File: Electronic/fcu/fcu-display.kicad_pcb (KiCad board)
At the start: 2 copper layers, 34 parts, among them U101 Connector-FPC-50pins

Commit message: Update fcu schemas and libraries
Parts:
- removed ALT201, ALT202, ALT203, ALT204, ALT205, HDG301, HDG302, HDG303, SPEED201, SPEED202, SPEED203, VS301, VS302, VS303, VS304, VS305: HDSP-7403, Display_7Segment:HDSP-7401
- added ALT1: HDSP-7401, Display_7Segment:HDSP-7401, F.Cu at (171.4, 63.5)
- added ALT2: HDSP-7401, Display_7Segment:HDSP-7401, F.Cu at (179.7, 63.5)
- added ALT3: HDSP-7401, Display_7Segment:HDSP-7401, F.Cu at (188.0, 63.5)
- added ALT4: HDSP-7401, Display_7Segment:HDSP-7401, F.Cu at (196.2, 63.5)
- added ALT5: HDSP-7401, Display_7Segment:HDSP-7401, F.Cu at (204.5, 63.5)
- added HDG1: HDSP-7401, Display_7Segment:HDSP-7401, F.Cu at (98.4, 63.5)
- added HDG2: HDSP-7401, Display_7Segment:HDSP-7401, F.Cu at (106.7, 63.5)
- added HDG3: HDSP-7401, Display_7Segment:HDSP-7401, F.Cu at (114.9, 63.5)
- added SPEED1: HDSP-7401, Display_7Segment:HDSP-7401, F.Cu at (61.0, 63.5)
- added SPEED2: HDSP-7401, Display_7Segment:HDSP-7401, F.Cu at (69.2, 63.5)
- added SPEED3: HDSP-7401, Display_7Segment:HDSP-7401, F.Cu at (77.5, 63.5)
- added VS1: HDSP-7401, Display_7Segment:HDSP-7401, F.Cu at (216.5, 63.5)
- added VS2: HDSP-7401, Display_7Segment:HDSP-7401, F.Cu at (224.8, 63.5)
- added VS3: HDSP-7401, Display_7Segment:HDSP-7401, F.Cu at (233.0, 63.5)
- added VS4: HDSP-7401, Display_7Segment:HDSP-7401, F.Cu at (241.3, 63.5)
- added VS5: HDSP-7401, Display_7Segment:HDSP-7401, F.Cu at (249.6, 63.5)
- moved DAltManaged401 0.64 mm to (212.7, 69.8)
- renumbered PadALT401 to PadALT1, PaveFPA401 to PadFPA1, PaveFPA402 to PadFPA2, PaveHDG401 to PadHDG1, PaveHDG402 to PadHDG2, PadLVLCH401 to PadLVLCH1, PadLine401 to PadLine1, PadLine402 to PadLine2, PaveMach401 to PadMach1, PaveSpeed401 to PadSpeed1, PaveTRK401 to PadTRK1, PaveTRK402 to PadTRK2, PaveVS401 to PadVS1, PaveVS402 to PadVS2
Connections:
- PadSpeed1 pad 3: Dr3SegA -> Net-(PadSpeed1-Pad3)
- PadSpeed1 pad 6: Dr3SegA -> Net-(PadSpeed1-Pad3)
- U101 pad 1: hdgVsDig3 -> Net-(U101-Pad1)
- U101 pad 10: Dr3Dig5 -> Dr3Dig0
- U101 pad 11: Dr3Dig6 -> Dr3SegDP
- U101 pad 12: Dr3Dig7 -> Dr3SegG
- U101 pad 13: speedAltDig3 -> Dr3SegF
- U101 pad 14: speedAltDig4 -> Dr3SegE
- U101 pad 15: speedAltDig5 -> Dr3SegD
- U101 pad 16: speedAltDig6 -> Dr3SegC
- U101 pad 17: speedAltDig7 -> Dr3SegB
- U101 pad 18: hdgVsB -> Dr3SegA
- U101 pad 19: hdgVsC -> speedAltE
- U101 pad 2: hdgVsDig4 -> Net-(U101-Pad2)
- U101 pad 20: hdgVsD -> speedAltD
- U101 pad 21: hdgVsE -> speedAltC
- U101 pad 22: hdgVsF -> speedAltB
- U101 pad 23: hdgVsG -> speedAltA
- U101 pad 24: hdgVsDP -> hdgVsDig2
- U101 pad 25: hdgVsDig0 -> hdgVsDig1
- U101 pad 26: hdgVsDig1 -> hdgVsDig0
- U101 pad 27: hdgVsDig2 -> hdgVsDP
- U101 pad 28: speedAltA -> hdgVsG
- U101 pad 29: speedAltB -> hdgVsF
- U101 pad 3: hdgVsDig5 -> speedAltDig2
- U101 pad 30: speedAltC -> hdgVsE
- U101 pad 31: speedAltD -> hdgVsD
- U101 pad 32: speedAltE -> hdgVsC
- U101 pad 33: Dr3SegA -> hdgVsB
- U101 pad 34: Dr3SegB -> speedAltDig7
- U101 pad 35: Dr3SegC -> speedAltDig6
- U101 pad 36: Dr3SegD -> speedAltDig5
- U101 pad 37: Dr3SegE -> speedAltDig4
- U101 pad 38: Dr3SegF -> speedAltDig3
- U101 pad 39: Dr3SegG -> Dr3Dig7
- U101 pad 4: hdgVsDig6 -> speedAltDig1
- U101 pad 40: Dr3SegDP -> Dr3Dig6
- U101 pad 41: Dr3Dig0 -> Dr3Dig5
- U101 pad 42: Dr3Dig1 -> speedAltDP
- U101 pad 43: Dr3Dig2 -> speedAltG
- U101 pad 44: Dr3Dig3 -> speedAltF
- U101 pad 45: Dr3Dig4 -> hdgVsA
- U101 pad 46: speedAltDig0 -> hdgVsDig7
- U101 pad 47: speedAltDig1 -> hdgVsDig6
- U101 pad 48: speedAltDig2 -> hdgVsDig5
- U101 pad 49: Net-(U101-Pad49) -> hdgVsDig4
- U101 pad 5: hdgVsDig7 -> speedAltDig0
- U101 pad 50: Net-(U101-Pad50) -> hdgVsDig3
- U101 pad 6: hdgVsA -> Dr3Dig4
- U101 pad 7: speedAltF -> Dr3Dig3
- U101 pad 8: speedAltG -> Dr3Dig2
- U101 pad 9: speedAltDP -> Dr3Dig1
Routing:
- net Dr3Dig0: track 369.3 -> 0.00 mm
- net speedAltF: track 218.3 -> 0.00 mm, vias 1 -> 0
- net hdgVsA: track 214.8 -> 0.00 mm, vias 1 -> 0
- net Dr3Dig1: track 214.1 -> 0.00 mm, vias 1 -> 0
- net hdgVsD: track 205.8 -> 0.00 mm, vias 2 -> 0
- net hdgVsF: track 204.3 -> 0.00 mm, vias 2 -> 0
- net Dr3SegF: track 198.4 -> 0.00 mm, vias 1 -> 0
- net hdgVsC: track 198.4 -> 0.00 mm
- net hdgVsG: track 197.0 -> 0.00 mm, vias 2 -> 0
- net hdgVsDP: track 194.1 -> 0.00 mm, vias 2 -> 0
- net hdgVsE: track 192.3 -> 0.00 mm, vias 2 -> 0
- net hdgVsB: track 191.7 -> 0.00 mm
- net speedAltG: track 184.0 -> 0.00 mm, vias 1 -> 0
- net speedAltD: track 176.2 -> 0.00 mm, vias 1 -> 0
- net speedAltC: track 175.0 -> 0.00 mm, vias 1 -> 0
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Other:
- board outline added: 205 x 30 mm
- board text added: "HomeCockpit A320 - VirtualGit FCU Display - V1.0 - 17/02/2021"

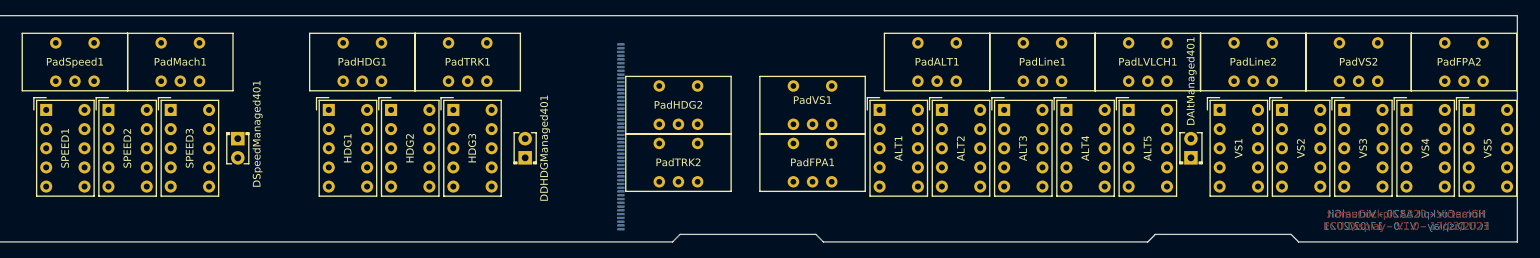
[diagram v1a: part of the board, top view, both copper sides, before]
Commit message: Update FCU display board with routing
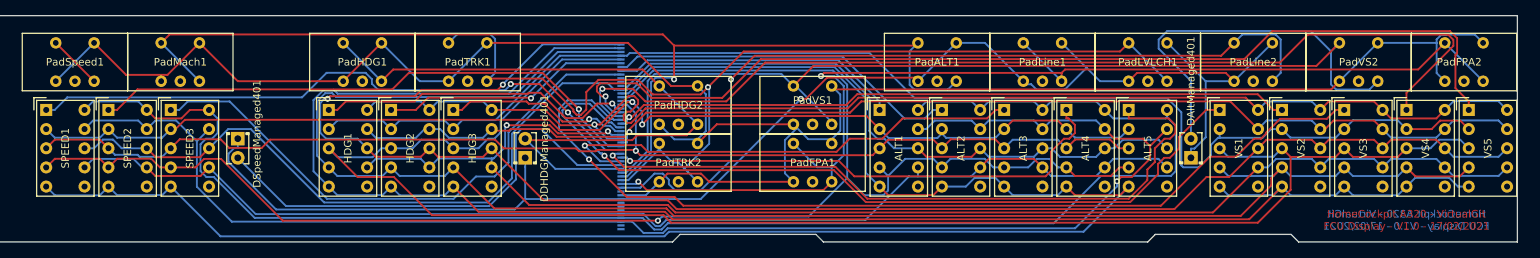
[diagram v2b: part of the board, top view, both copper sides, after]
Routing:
- net Dr3Dig0: track 0.00 -> 273.5 mm
- net speedAltDig4: track 0.00 -> 235.9 mm
- net hdgVsDig4: track 0.00 -> 225.0 mm
- net hdgVsDig5: track 0.00 -> 223.8 mm
- net hdgVsDig7: track 0.00 -> 221.0 mm
- net hdgVsDig3: track 0.00 -> 217.6 mm, vias 0 -> 2
- net speedAltDig1: track 0.00 -> 209.0 mm
- net speedAltDig5: track 0.00 -> 205.4 mm, vias 0 -> 1
- net speedAltDig2: track 0.00 -> 198.5 mm, vias 0 -> 1
- net Dr3Dig1: track 0.00 -> 194.3 mm, vias 0 -> 1
- net hdgVsDig0: track 0.00 -> 183.7 mm, vias 0 -> 2
- net hdgVsDig6: track 0.00 -> 174.5 mm
- net speedAltDig3: track 0.00 -> 173.5 mm
- net hdgVsDig1: track 0.00 -> 171.6 mm, vias 0 -> 1
- net Dr3SegC: track 0.00 -> 168.8 mm
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
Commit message: Adust fcu display pcb layout Add Vcc to rotary encoder and update pcb with jst +1 pin
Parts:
- moved PadMach1 8.98 mm to (69.8, 58.4)
- moved PadSpeed1 8.98 mm to (55.9, 58.4)
- moved PadFPA2 8.28 mm to (257.2, 57.8)
- moved PadLine2 8.28 mm to (229.2, 57.8)
- moved PadVS2 8.28 mm to (243.2, 57.8)
- moved PadALT1 8.28 mm to (187.3, 57.8)
- moved PadLVLCH1 8.28 mm to (215.3, 57.8)
- moved PadLine1 8.28 mm to (201.3, 57.8)
- moved SPEED2 7.62 mm to (61.6, 63.5)
- moved SPEED3 7.62 mm to (69.8, 63.5)
- moved SPEED1 7.62 mm to (53.3, 63.5)
- moved DSpeedManaged401 6.98 mm to (79.4, 67.3)
- moved VS3 6.35 mm to (239.4, 63.5)
- moved VS1 6.35 mm to (222.9, 63.5)
- moved VS2 6.35 mm to (231.1, 63.5)
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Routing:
- net Dr3Dig0: track 273.5 -> 0.00 mm
- net speedAltDig4: track 235.9 -> 0.00 mm
- net hdgVsDig4: track 225.0 -> 0.00 mm
- net hdgVsDig5: track 223.8 -> 0.00 mm
- net hdgVsDig7: track 221.0 -> 0.00 mm
- net hdgVsDig3: track 217.6 -> 0.00 mm, vias 2 -> 0
- net speedAltDig1: track 209.0 -> 0.00 mm
- net speedAltDig5: track 205.4 -> 0.00 mm, vias 1 -> 0
- net speedAltDig2: track 198.5 -> 0.00 mm, vias 1 -> 0
- net Dr3Dig1: track 194.3 -> 0.00 mm, vias 1 -> 0
- net hdgVsDig0: track 183.7 -> 0.00 mm, vias 2 -> 0
- net hdgVsDig6: track 174.5 -> 0.00 mm
- net speedAltDig3: track 173.5 -> 0.00 mm
- net hdgVsDig1: track 171.6 -> 0.00 mm, vias 1 -> 0
- net Dr3SegC: track 168.8 -> 0.00 mm
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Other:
- board size 205 x 30 mm -> 238 x 28 mm
- board text added: "HomeCockpit A320 - VirtualGit - FCU Display - V1.0 - 17/02/2021"
- board text removed: "HomeCockpit A320 - VirtualGit FCU Display - V1.0 - 17/02/2021"

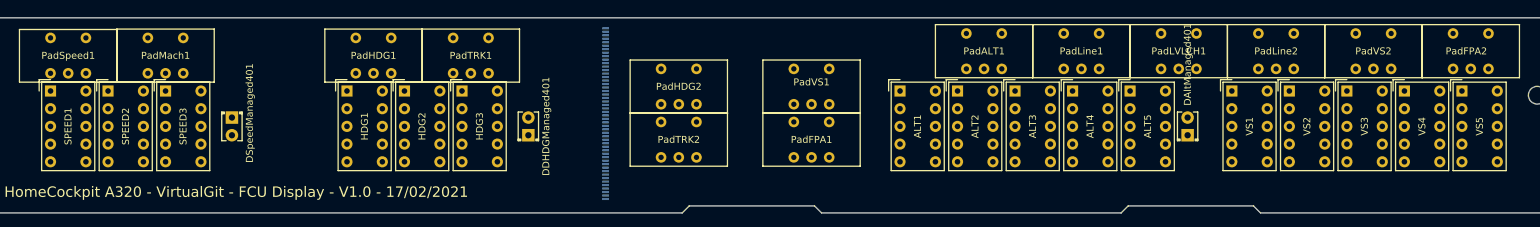
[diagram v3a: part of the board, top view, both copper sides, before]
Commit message: Update FCU PCB net routing
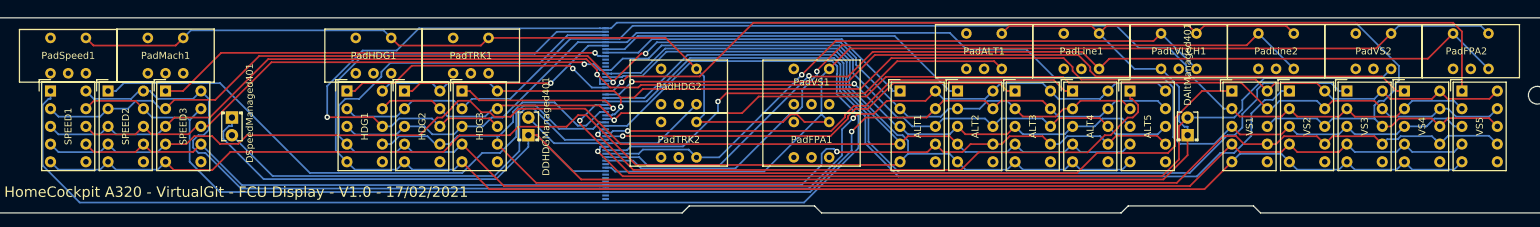
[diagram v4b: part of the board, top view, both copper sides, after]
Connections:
- PadALT1 pad 3: Dr3SegD -> Net-(PadALT1-Pad3)
- PadALT1 pad 4: Dr3Dig1 -> Net-(PadALT1-Pad4)
- PadFPA1 pad 3: Dr3SegF -> Net-(PadFPA1-Pad3)
- PadFPA1 pad 4: Dr3Dig0 -> Net-(PadFPA1-Pad4)
- PadFPA1 pad 6: Dr3SegF -> Net-(PadFPA1-Pad6)
- PadFPA2 pad 4: Dr3Dig0 -> Net-(PadFPA2-Pad4)
- PadHDG1 pad 3: Dr3SegB -> Net-(PadHDG1-Pad3)
- PadHDG1 pad 4: Dr3Dig0 -> Net-(PadHDG1-Pad4)
- PadHDG1 pad 6: Dr3SegB -> Net-(PadHDG1-Pad6)
- PadHDG2 pad 3: Dr3SegB -> Net-(PadHDG2-Pad3)
- PadHDG2 pad 4: Dr3Dig0 -> Net-(PadHDG2-Pad4)
- PadLine1 pad 3: Dr3SegF -> Net-(PadLine1-Pad3)
- PadLine1 pad 4: Dr3Dig1 -> Net-(PadLine1-Pad4)
- PadLine2 pad 4: Dr3Dig1 -> Net-(PadLine2-Pad4)
- PadMach1 pad 3: Dr3SegD -> Net-(PadMach1-Pad3)
- PadMach1 pad 4: Dr3Dig0 -> Net-(PadMach1-Pad4)
- PadMach1 pad 6: Dr3SegD -> Net-(PadMach1-Pad6)
- PadSpeed1 pad 4: Dr3Dig0 -> Net-(PadSpeed1-Pad4)
- PadSpeed1 pad 6: Net-(PadSpeed1-Pad3) -> Net-(PadSpeed1-Pad6)
- PadTRK1 pad 3: Dr3SegE -> Net-(PadTRK1-Pad3)
- PadTRK1 pad 4: Dr3Dig0 -> Net-(PadTRK1-Pad4)
- PadTRK1 pad 6: Dr3SegE -> Net-(PadTRK1-Pad6)
- PadTRK2 pad 3: Dr3SegE -> Net-(PadTRK2-Pad3)
- PadTRK2 pad 4: Dr3Dig0 -> Net-(PadTRK2-Pad4)
- PadVS1 pad 3: Dr3SegC -> Net-(PadVS1-Pad3)
- PadVS1 pad 4: Dr3Dig0 -> Net-(PadVS1-Pad4)
- PadVS1 pad 6: Dr3SegC -> Net-(PadVS1-Pad6)
- PadVS2 pad 3: Dr3SegC -> Net-(PadVS2-Pad3)
- PadVS2 pad 4: Dr3Dig0 -> Net-(PadVS2-Pad4)
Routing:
- net Dr3Dig0: track 0.00 -> 261.4 mm
- net hdgVsDig3: track 0.00 -> 237.7 mm, vias 0 -> 1
- net Dr3Dig1: track 0.00 -> 235.3 mm
- net hdgVsDig4: track 0.00 -> 222.7 mm
- net speedAltDig4: track 0.00 -> 222.1 mm
- net hdgVsDig5: track 0.00 -> 219.5 mm
- net speedAltDig5: track 0.00 -> 219.5 mm
- net hdgVsDig0: track 0.00 -> 192.5 mm
- net speedAltB: track 0.00 -> 184.3 mm
- net hdgVsDig7: track 0.00 -> 183.0 mm
- net speedAltDig1: track 0.00 -> 182.0 mm, vias 0 -> 1
- net speedAltDig2: track 0.00 -> 176.9 mm, vias 0 -> 1
- net hdgVsDig6: track 0.00 -> 176.3 mm
- net hdgVsDig1: track 0.00 -> 174.8 mm, vias 0 -> 1
- net speedAltDig6: track 0.00 -> 173.4 mm, vias 0 -> 2
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
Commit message: Finalise first FCU PCB version
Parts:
- moved PadHDG1 0.64 mm to (99.7, 57.8)
- moved PadMach1 0.64 mm to (69.8, 57.8)
- moved PadSpeed1 0.64 mm to (55.9, 57.8)
- moved PadTRK1 0.64 mm to (113.7, 57.8)
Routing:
- net hdgVsDig7: track 183.0 -> 292.7 mm
- net speedAltB: track 184.3 -> 102.4 mm, vias 0 -> 1
- net hdgVsDig6: track 176.3 -> 231.1 mm, vias 0 -> 1
- net Dr3SegF: track 139.2 -> 187.6 mm
- net hdgVsDig3: track 237.7 -> 275.8 mm, vias 1 -> 0
- net Dr3Dig1: track 235.3 -> 211.6 mm, vias 0 -> 1
- net hdgVsDig2: track 172.5 -> 192.5 mm, vias 1 -> 0
- net Dr3Dig0: track 261.4 -> 276.2 mm
- net hdgVsDig5: track 219.5 -> 205.7 mm, vias 0 -> 1
- net speedAltDig3: track 172.3 -> 186.0 mm
- net hdgVsDig0: track 192.5 -> 179.7 mm, vias 0 -> 2
- net Dr3SegB: track 28.0 -> 37.5 mm
- net speedAltA: track 84.9 -> 94.5 mm
- net speedAltC: track 88.5 -> 80.3 mm
- net Dr3SegG: track 111.2 -> 117.9 mm
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- added copper zone on B.Cu, net (none)
- added copper zone on F.Cu, net (none)

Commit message: Update electornic schema of FCU MotherBoard and Display. Replace MAX7219 for leds to dedicated TLC5917.
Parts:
- removed U101: Connector-FPC-50pins, home-cockpit-footprints:Connector-FPC-50pins-0.5mm
- added DisplayConnector1: Connector-FPC-50pins, home-cockpit-footprints:Connector-FPC-50pins-0.5mm, B.Cu at (136.5, 66.7)
- added PadLAT1: LedPad, home-cockpit-footprints:PadLed-KingBright-DE-2YD, F.Cu at (123.2, 57.8)
- PadALT1, PadFPA1, PadFPA2, PadHDG1, PadHDG2, PadLVLCH1, PadLine1, PadLine2, PadMach1, PadSpeed1, PadTRK1, PadTRK2, PadVS1, PadVS2: value LedPave-home-cockpit-library -> LedPad
- moved PadTRK1 4.45 mm to (109.2, 57.8)
- moved PadHDG1 4.44 mm to (95.2, 57.8)
- moved DSpeedManaged401 1.91 mm to (79.4, 69.2), turned to 90 degrees
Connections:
- DAltManaged401 pad 1: Dr3Dig1 -> LedManagedALT
- DAltManaged401 pad 2: Dr3SegC -> Vcc12V
- DDHDGManaged401 pad 1: Dr3Dig1 -> LedManagedHDG
- DDHDGManaged401 pad 2: Dr3SegB -> Vcc12V
- DSpeedManaged401 pad 1: Dr3Dig1 -> LedManagedSpeed
- DSpeedManaged401 pad 2: Dr3SegA -> Vcc12V
- PadALT1 pad 1: Dr3Dig1 -> Net-(PadALT1-Pad1)
- PadALT1 pad 3: Net-(PadALT1-Pad3) -> Vcc12V
- PadALT1 pad 6: Dr3SegD -> Net-(PadALT1-Pad4)
- PadFPA1 pad 1: Dr3Dig0 -> Net-(PadFPA1-Pad1)
- PadFPA1 pad 3: Net-(PadFPA1-Pad3) -> Vcc12V
- PadFPA1 pad 6: Net-(PadFPA1-Pad6) -> Net-(PadFPA1-Pad4)
- PadFPA2 pad 1: Dr3Dig0 -> LedPadFPA
- PadFPA2 pad 3: Dr3SegF -> Net-(PadFPA1-Pad1)
- PadFPA2 pad 6: Dr3SegF -> Net-(PadFPA2-Pad4)
- PadHDG1 pad 1: Dr3Dig0 -> Net-(PadHDG1-Pad1)
- PadHDG1 pad 3: Net-(PadHDG1-Pad3) -> Vcc12V
- PadHDG1 pad 6: Net-(PadHDG1-Pad6) -> Net-(PadHDG1-Pad4)
- PadHDG2 pad 1: Dr3Dig0 -> LedPadHDG
- PadHDG2 pad 3: Net-(PadHDG2-Pad3) -> Net-(PadHDG1-Pad1)
- PadHDG2 pad 6: Dr3SegB -> Net-(PadHDG2-Pad4)
- PadLVLCH1 pad 1: Dr3Dig1 -> LedPadStaticALT
- PadLVLCH1 pad 3: Dr3SegE -> Net-(PadALT1-Pad1)
- PadLVLCH1 pad 4: Dr3Dig1 -> Net-(PadLVLCH1-Pad4)
- PadLVLCH1 pad 6: Dr3SegE -> Net-(PadLVLCH1-Pad4)
- PadLine1 pad 1: Dr3Dig1 -> Net-(PadLine1-Pad1)
- PadLine1 pad 3: Net-(PadLine1-Pad3) -> Vcc12V
- PadLine1 pad 6: Dr3SegF -> Net-(PadLine1-Pad4)
- PadLine2 pad 1: Dr3Dig1 -> LedPadStaticLines
- PadLine2 pad 3: Dr3SegG -> Net-(PadLine1-Pad1)
- PadLine2 pad 6: Dr3SegG -> Net-(PadLine2-Pad4)
- PadMach1 pad 1: Dr3Dig0 -> LedPadMACH
- PadMach1 pad 3: Net-(PadMach1-Pad3) -> Vcc12V
- PadMach1 pad 6: Net-(PadMach1-Pad6) -> Net-(PadMach1-Pad4)
- PadSpeed1 pad 1: Dr3Dig0 -> LedPadSPD
- PadSpeed1 pad 3: Net-(PadSpeed1-Pad3) -> Vcc12V
- PadSpeed1 pad 6: Net-(PadSpeed1-Pad6) -> Net-(PadSpeed1-Pad4)
- PadTRK1 pad 1: Dr3Dig0 -> Net-(PadTRK1-Pad1)
- PadTRK1 pad 3: Net-(PadTRK1-Pad3) -> Vcc12V
- PadTRK1 pad 6: Net-(PadTRK1-Pad6) -> Net-(PadTRK1-Pad4)
- PadTRK2 pad 1: Dr3Dig0 -> LedPadTRK
- PadTRK2 pad 3: Net-(PadTRK2-Pad3) -> Net-(PadTRK1-Pad1)
- PadTRK2 pad 6: Dr3SegE -> Net-(PadTRK2-Pad4)
- PadVS1 pad 1: Dr3Dig0 -> Net-(PadVS1-Pad1)
- PadVS1 pad 3: Net-(PadVS1-Pad3) -> Vcc12V
- PadVS1 pad 6: Net-(PadVS1-Pad6) -> Net-(PadVS1-Pad4)
- PadVS2 pad 1: Dr3Dig0 -> LedPadVS
- PadVS2 pad 3: Net-(PadVS2-Pad3) -> Net-(PadVS1-Pad1)
- PadVS2 pad 6: Dr3SegC -> Net-(PadVS2-Pad4)
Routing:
- net Dr3Dig0: track 276.2 -> 0.00 mm
- net Vcc12V: track 0.00 -> 253.9 mm, vias 0 -> 3
- net Dr3Dig1: track 211.6 -> 0.00 mm, vias 1 -> 0
- net Dr3SegF: track 187.6 -> 0.00 mm, vias 1 -> 0
- net LedPadFPA: track 0.00 -> 125.2 mm, vias 0 -> 1
- net Dr3SegC: track 124.7 -> 0.00 mm, vias 1 -> 0
- net Dr3SegG: track 117.9 -> 0.00 mm, vias 1 -> 0
- net speedAltDig7: track 167.7 -> 284.9 mm
- net speedAltDig4: track 219.9 -> 333.2 mm, vias 0 -> 1
- net LedPadVS: track 0.00 -> 112.7 mm, vias 0 -> 1
- net hdgVsDig3: track 275.8 -> 174.3 mm
- net Dr3SegE: track 100.9 -> 0.00 mm, vias 1 -> 0
- net LedPadStaticLines: track 0.00 -> 97.5 mm
- net LedManagedALT: track 0.00 -> 96.6 mm
- net Net-(PadFPA1-Pad1): track 0.00 -> 95.8 mm, vias 0 -> 1
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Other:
- board size 238 x 28 mm -> 238 x 32.4 mm
- board text added: "HomeCockpit A320 - VirtualGit - FCU Display - V2.0 - 09/04/2021"
- board text removed: "HomeCockpit A320 - VirtualGit - FCU Display - V1.0 - 17/02/2021"
